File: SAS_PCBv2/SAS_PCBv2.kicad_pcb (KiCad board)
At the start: 2 copper layers, 107.5 x 71 mm, 53 parts, among them J1 GY-BMP280, J10 Conn_01x04, J11 Conn_01x04, J12 GY-GPS6MV2, J14 Fan PWM, J16 GT17HN-4DP-2HD56, J17 GT17HN-4DP-2HD56, J2 Raspberry Pi 4 Model B, J3 Conn_01x02_Pin, J4 Conn_01x02, J5 Conn_01x02, J6 Conn_01x02, J7 Conn_01x02, J8 Conn_01x02, J9 Conn_01x02, Q2 2N4403, Q3 2N4403, Q4 BS170, Q5 BS170, SW1 SW_SPST, U2 LF33_TO220

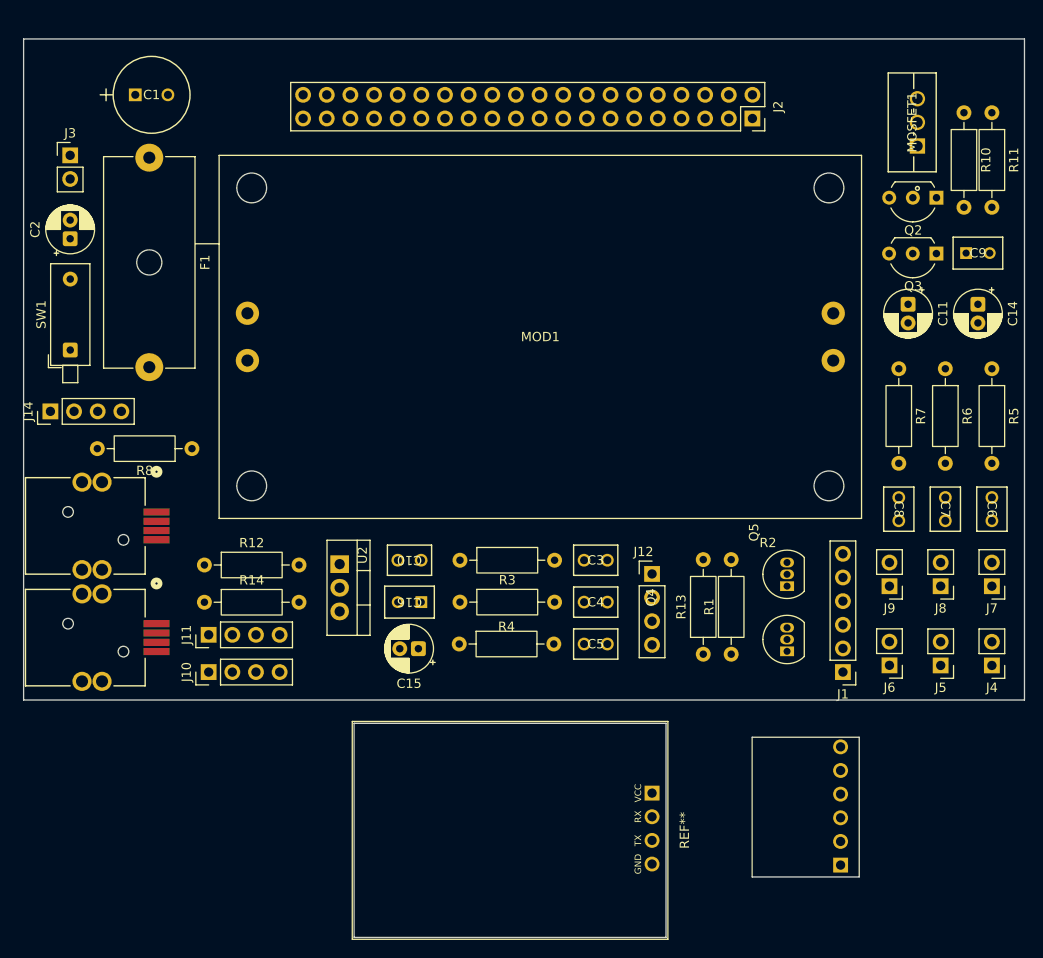
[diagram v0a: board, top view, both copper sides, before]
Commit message: Finalisation du PCB : routage complet, découpe du contour, DRC?
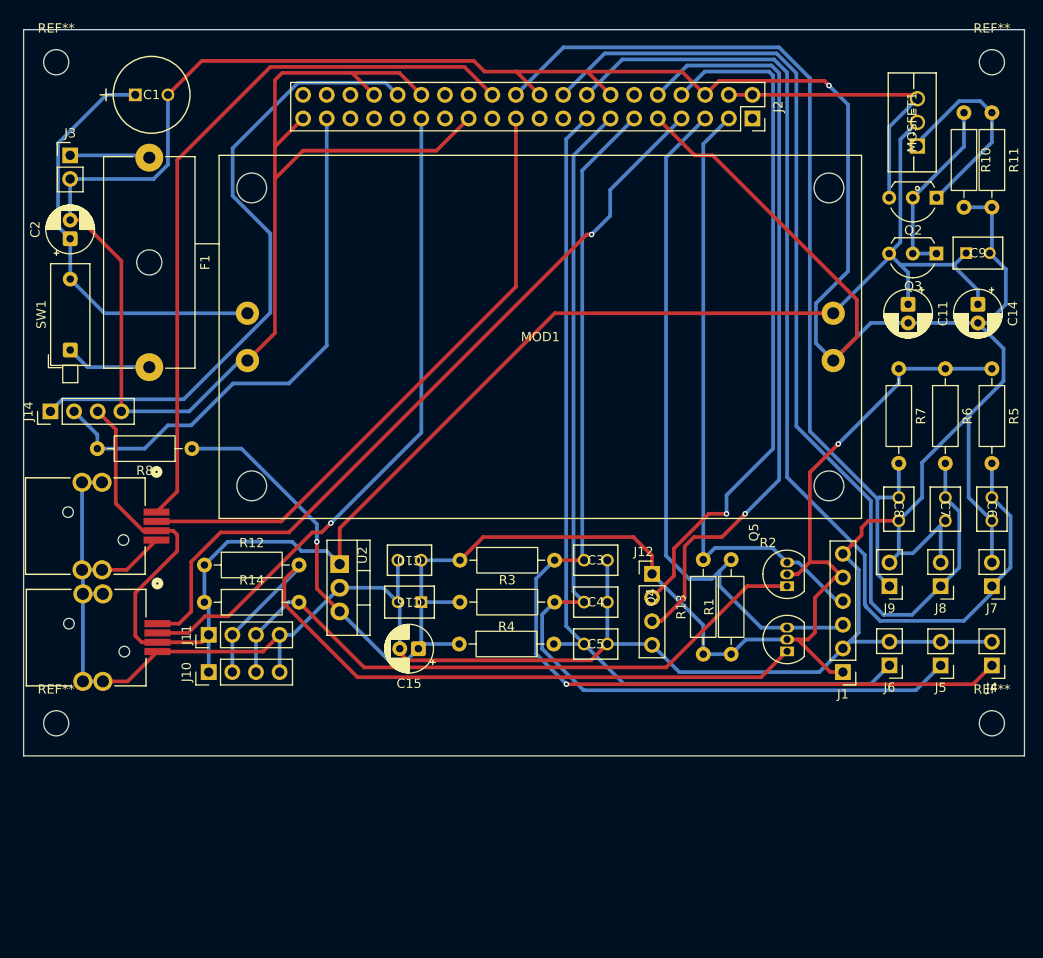
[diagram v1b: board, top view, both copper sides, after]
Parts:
- removed the REF** at (199.5, 118.5)
- removed the REF** at (208.8, 135.0)
- added REF**: MountingHole_2.7mm_M2.5, MountingHole:MountingHole_2.7mm_M2.5, F.Cu at (234.5, 47.5)
- added REF**: MountingHole_2.7mm_M2.5, MountingHole:MountingHole_2.7mm_M2.5, F.Cu at (134.0, 47.5)
- added REF**: MountingHole_2.7mm_M2.5, MountingHole:MountingHole_2.7mm_M2.5, F.Cu at (134.0, 118.5)
- added REF**: MountingHole_2.7mm_M2.5, MountingHole:MountingHole_2.7mm_M2.5, F.Cu at (234.5, 118.5)
- moved J16 12.0 mm to (138.1, 109.5)
- moved J17 12.0 mm to (138.0, 97.5)
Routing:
- net GND: track 0.00 -> 570.9 mm, vias 0 -> 1
- net +5V: track 0.00 -> 178.0 mm
- net +3V3: track 0.00 -> 165.1 mm, vias 0 -> 2
- net BTN_4: track 0.00 -> 115.5 mm
- net BTN_1: track 0.00 -> 115.0 mm, vias 0 -> 1
- net BTN_5: track 0.00 -> 111.9 mm
- net BTN_2: track 0.00 -> 108.5 mm
- net BTN_6: track 0.00 -> 99.2 mm
- net BTN_3: track 0.00 -> 96.8 mm
- net UART_RAD1_RX: track 0.00 -> 83.5 mm, vias 0 -> 1
- net UART_GPS_TX: track 0.00 -> 81.5 mm, vias 0 -> 1
- net UART_RAD2_RX: track 0.00 -> 78.0 mm
- net I2C_5V_SCL: track 0.00 -> 77.7 mm
- net I2C_3V3_SCL: track 0.00 -> 74.4 mm
- net UART_GPS_RX: track 0.00 -> 73.6 mm, vias 0 -> 1
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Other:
- board size 107.5 x 71 mm -> 107.5 x 78 mm

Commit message: Rerouting des traces débutant du top layer
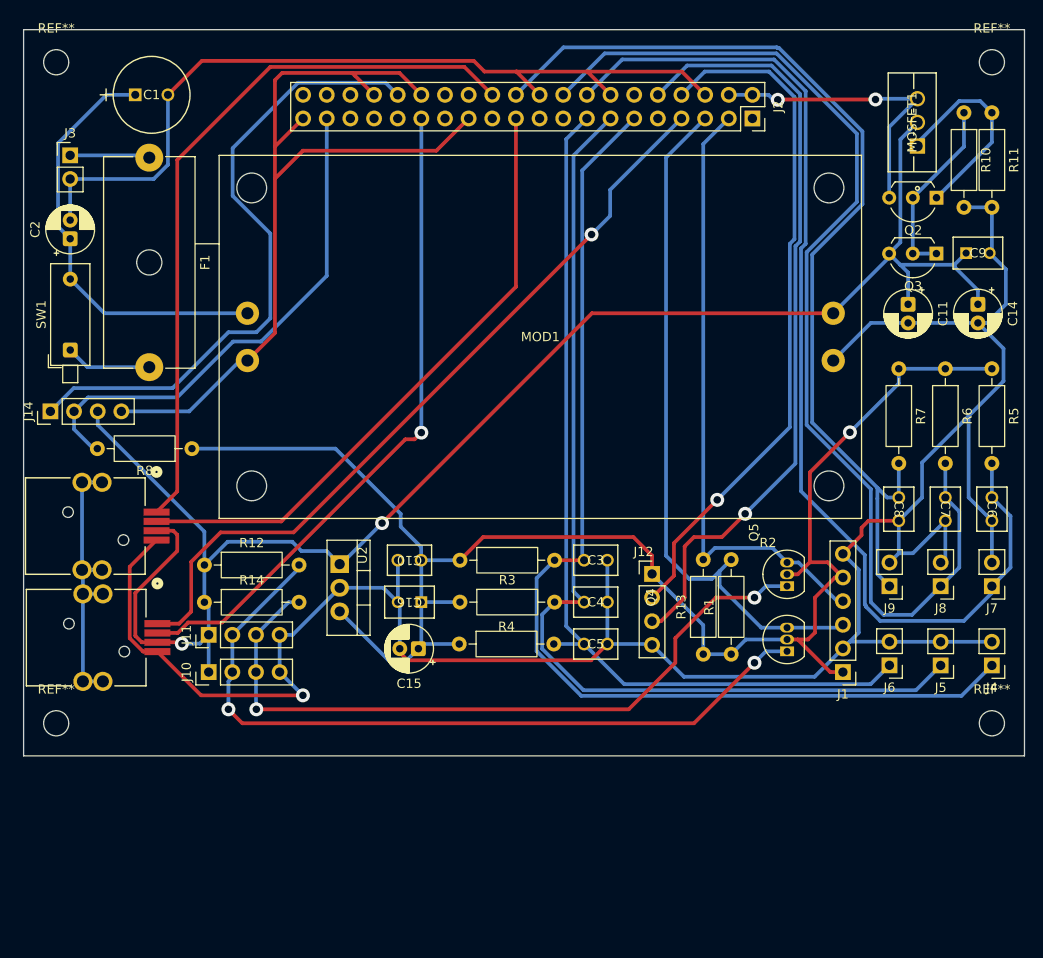
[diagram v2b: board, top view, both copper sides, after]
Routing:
- net GND: track 570.9 -> 472.2 mm
- net I2C_5V_SDA: track 69.0 -> 78.1 mm, vias 0 -> 2
- net BTN_6: track 99.2 -> 104.0 mm
- net I2C_5V_SCL: track 77.7 -> 82.5 mm, vias 0 -> 2
- net BTN_5: track 111.9 -> 116.3 mm
- net +3V3: track 165.1 -> 169.1 mm, vias 2 -> 1
- net FAN_TACH: track 58.7 -> 55.4 mm
- net +5V: track 178.0 -> 180.8 mm, vias 0 -> 2
- net UART_GPS_TX: track 81.5 -> 83.4 mm
- net BTN_1: track 115.0 -> 115.8 mm, vias 1 -> 0
- net UART_GPS_RX: track 73.6 -> 74.4 mm
- net RPI_5V: track 32.3 -> 32.4 mm, vias 0 -> 2

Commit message: Routage des connexions du côté de la soudure et ajout d'un plan de masse
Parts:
- moved J4 11.0 mm to (223.5, 112.3)
- moved J6 11.0 mm to (234.5, 112.3)
- moved J7 11.0 mm to (223.5, 103.8)
- moved J9 11.0 mm to (234.5, 103.8)
- moved C6 10.0 mm to (224.5, 94.2)
- moved C8 10.0 mm to (234.5, 94.2)
- moved R5 10.0 mm to (224.5, 80.4)
- moved R7 10.0 mm to (234.5, 80.4)
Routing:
- net GND: track 472.2 -> 56.0 mm
- net BTN_4: track 115.9 -> 87.5 mm
- net +3V3: track 169.1 -> 191.1 mm, vias 1 -> 4
- net BTN_3: track 96.8 -> 115.5 mm
- net BTN_5: track 116.3 -> 98.6 mm
- net BTN_1: track 115.8 -> 103.1 mm
- net I2C_3V3_SDA: track 66.4 -> 77.0 mm
- net RPI_5V: track 32.4 -> 42.3 mm
- net BTN_6: track 104.0 -> 109.0 mm
- net FAN_TACH: track 55.4 -> 60.3 mm
- net I2C_3V3_SCL: track 74.4 -> 70.6 mm
- net +5V: track 180.8 -> 184.4 mm, vias 2 -> 3
- net Vent_PWM: track 68.9 -> 71.9 mm
- net UART_GPS_RX: track 74.4 -> 75.6 mm, vias 1 -> 2
- net I2C_5V_SDA: track 78.1 -> 77.2 mm
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- added copper zone on B.Cu, net GND

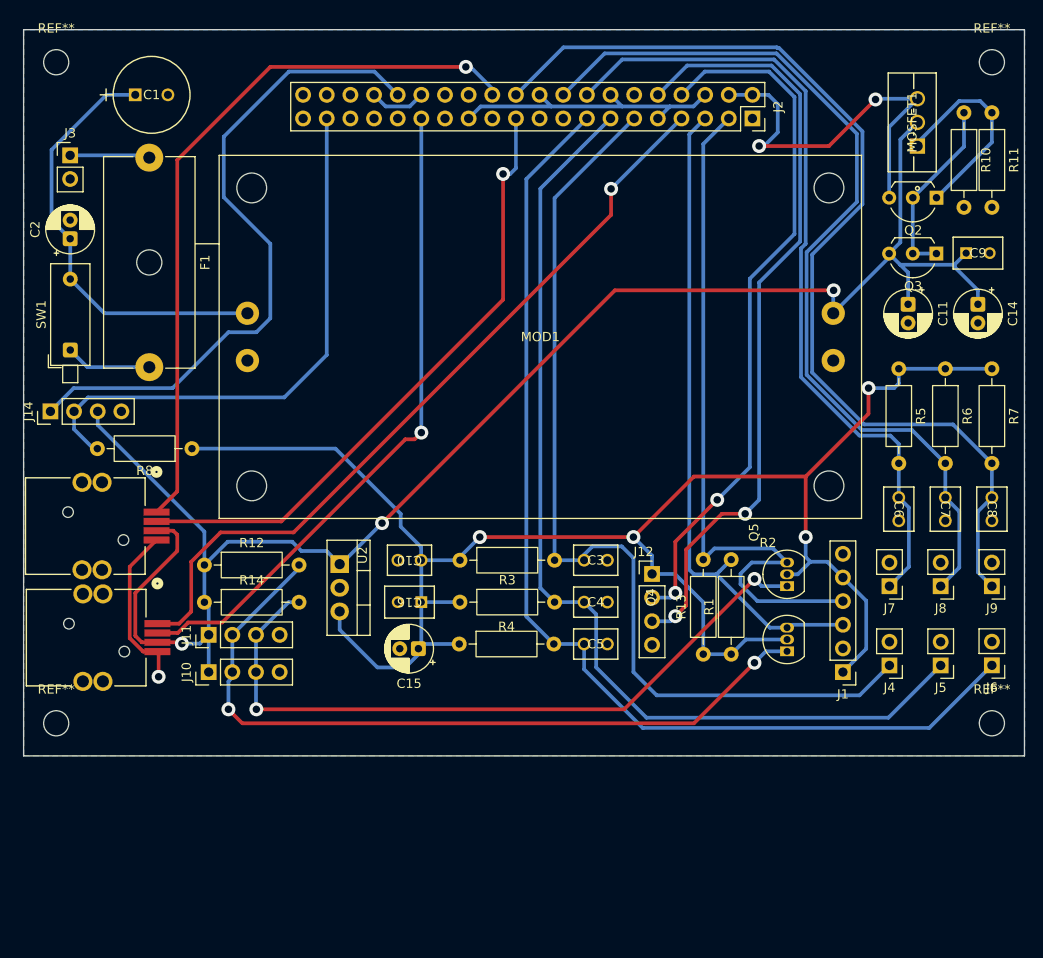
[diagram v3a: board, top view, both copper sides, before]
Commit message: Fix footprints, widen power traces, route RPi cables, fix transistor pinout
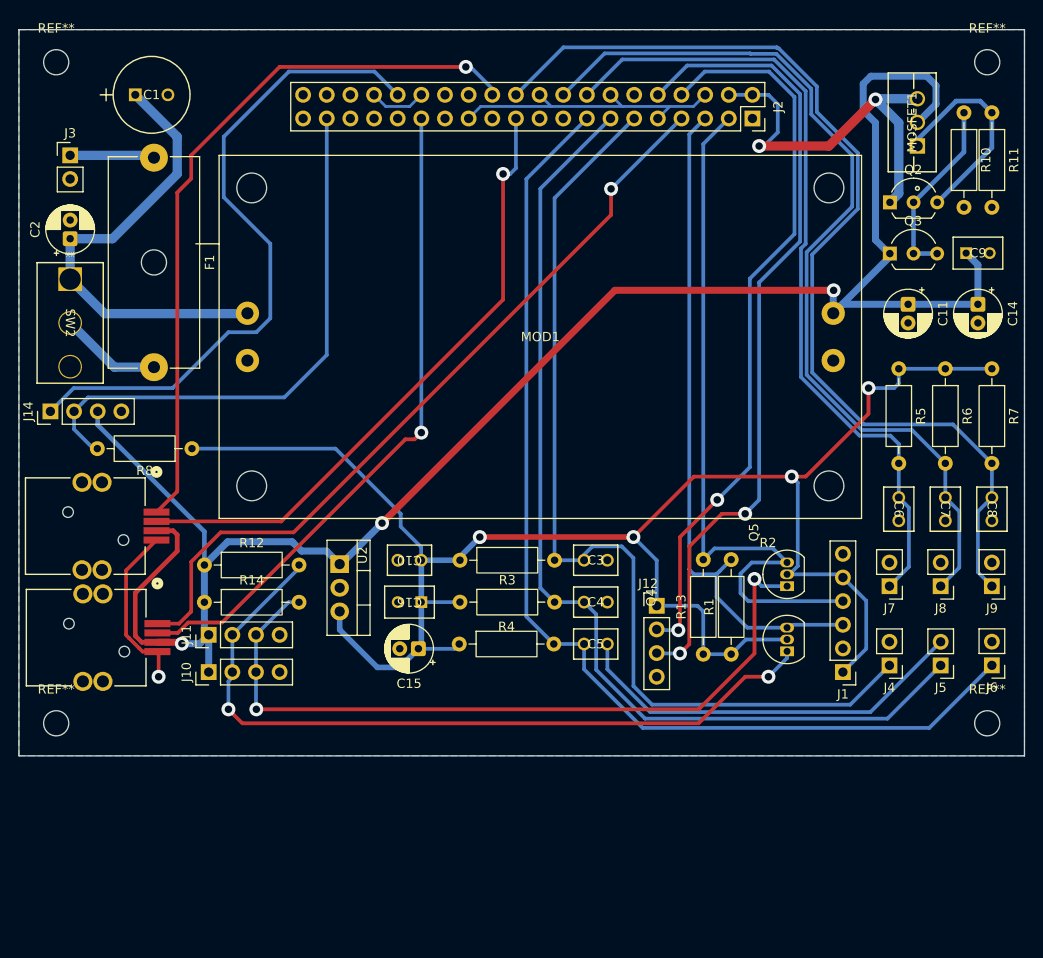
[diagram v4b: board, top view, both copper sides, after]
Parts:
- removed SW1: SW_SPST, Button_Switch_THT:SW_DIP_SPSTx01_Piano_10.8x4.1mm_W7.62mm_P2.54mm
- added SW2: SW_SPDT, SAS_PCBv2_footprint:SW_ANT1_CRS, F.Cu at (135.5, 70.8)
- moved Q2 5.02 mm to (223.6, 62.5), turned to 0 degrees
- moved Q3 5.00 mm to (223.5, 68.0), turned to 0 degrees
- moved J12 3.46 mm to (198.5, 105.9)
- moved F1 0.50 mm to (144.5, 57.8)
- moved REF** 0.50 mm to (234.0, 47.5)
- moved REF** 0.50 mm to (234.0, 118.5)
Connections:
- Q2 pad 1: Net-(MOSFET1-G) -> RPI_5V
- Q2 pad 3: RPI_5V -> Net-(MOSFET1-G)
- Q3 pad 1: Net-(Q2-B) -> +5V
- Q3 pad 3: +5V -> Net-(Q2-B)
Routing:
- net GND: track 56.0 -> 99.9 mm
- net +5V: track 184.4 -> 204.6 mm
- net I2C_5V_SDA: track 77.2 -> 81.9 mm
- net UART_GPS_TX: track 83.7 -> 87.3 mm
- net UART_GPS_RX: track 75.6 -> 79.1 mm
- net VIN: track 46.7 -> 49.7 mm
- net Net-(SW2-B): track 9.25 -> 11.0 mm
- net BTN_1: track 103.1 -> 104.8 mm
- net +3V3: track 191.1 -> 192.8 mm
- net I2C_3V3_SCL: track 70.6 -> 72.0 mm
- net Net-(MOSFET1-G): track 22.3 -> 23.0 mm
- net RPI_5V: track 42.3 -> 42.9 mm
- net UART_RAD2_RX: track 78.2 -> 77.6 mm
- net I2C_3V3_SDA: track 77.0 -> 77.6 mm
- net Net-(J3-Pin_1): track 8.60 -> 9.10 mm
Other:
- board size 107.5 x 78 mm -> 108 x 78 mm

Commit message: ajout Logo GAUL
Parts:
- added G***: LOGO, ODB:Logo-GAUL, F.Cu at (156.4, 130.1)
